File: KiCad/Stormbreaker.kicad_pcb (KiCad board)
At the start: 4 copper layers, 50.2 x 21 mm, 43 parts, among them J1 Micro_SD_Card_Det2, J2 USB_C_Receptacle_USB2.0_14P, J3 Conn_01x03, J4 FAN, Q1 PMOS, Q2 NMOS, SW1 SW_Push, U1 BQ25895RTW, U3 ATtiny1616-M

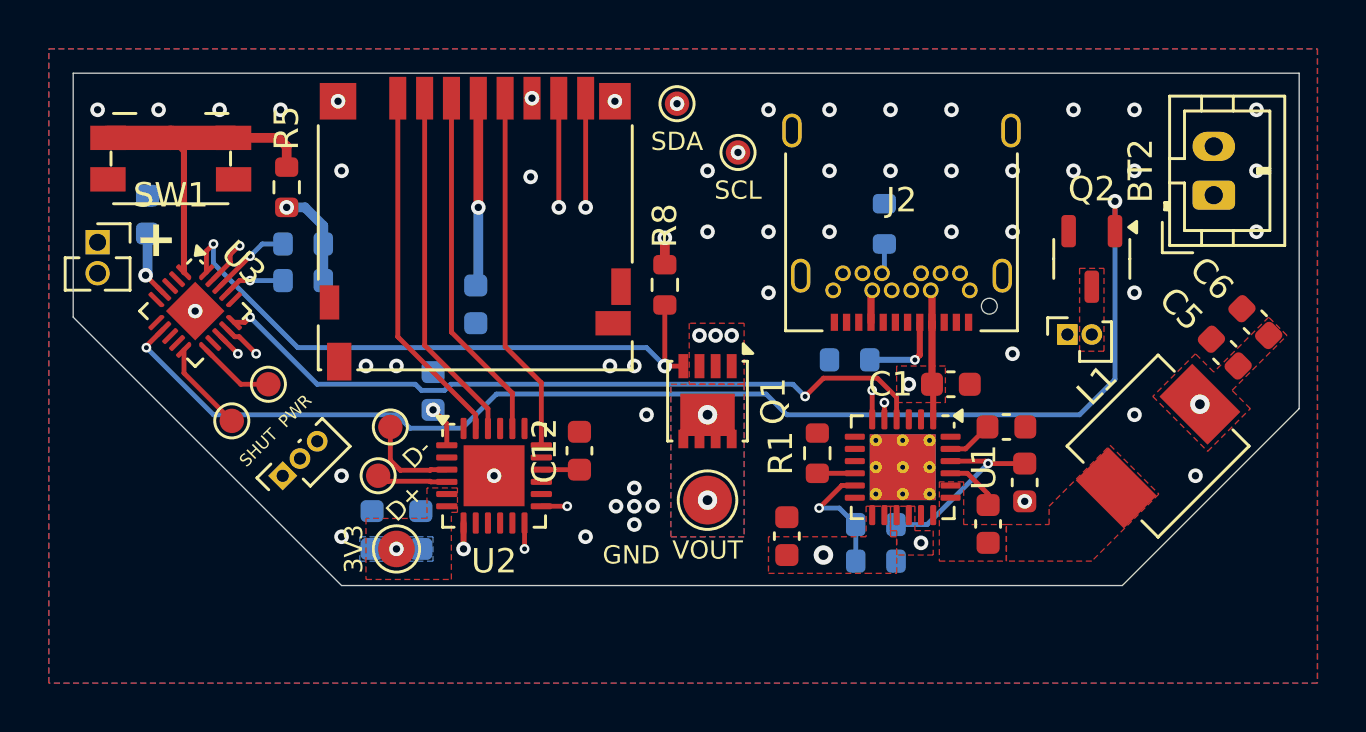
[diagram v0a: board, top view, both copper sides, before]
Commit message: More routing, via stitching, VCC zones
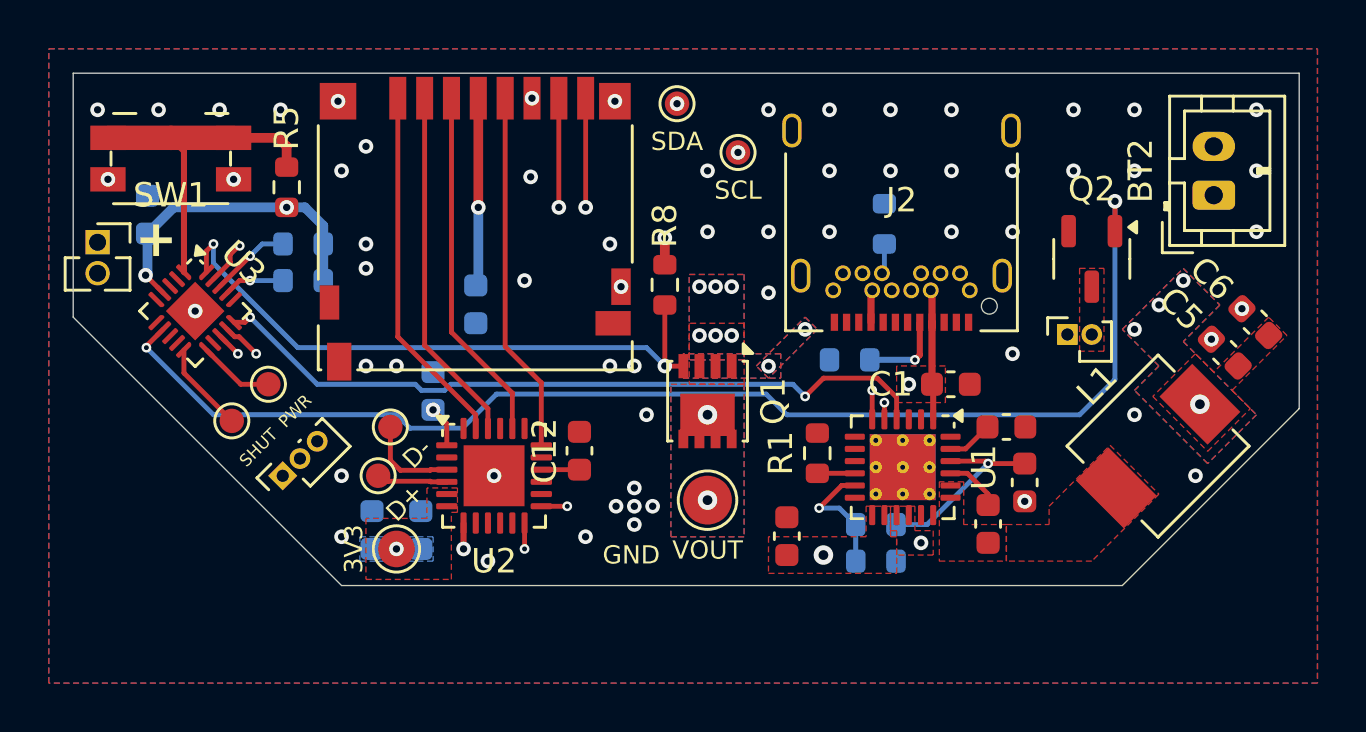
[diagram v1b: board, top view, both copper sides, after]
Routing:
- net VCC: track 7.99 -> 14.1 mm, vias 8 -> 16
- net GND: vias 51 -> 61
- added copper zone on B.Cu, net VCC
- added copper zone on In1.Cu, net VCC

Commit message: more misc changes
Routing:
- net /BATT: track 60.8 -> 61.8 mm
- net VCC: vias 16 -> 18
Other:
- outline, holes or cut-outs redrawn
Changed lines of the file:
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@@
 		(attr through_hole)
 		(fp_line
-			(start -1.33 0.635)
-			(end -1.33 1.965)
-			(stroke
-				(width 0.12)
-				(type solid)
-			)
-			(layer "F.SilkS")
-		)
-		(fp_line
-			(start -1.33 0.635)
-			(end -0.76 0.635)
-			(stroke
-				(width 0.12)
-				(type solid)
-			)
-			(layer "F.SilkS")
-		)
-		(fp_line
-			(start -1.33 1.965)
-			(end -0.30753 1.965)
-			(stroke
-				(width 0.12)
-				(type solid)
-			)
-			(layer "F.SilkS")
-		)
-		(fp_line
-			(start 0 -0.76)
-			(end 1.33 -0.76)
-			(stroke
-				(width 0.12)
-				(type solid)
-			)
-			(layer "F.SilkS")
-		)
-		(fp_line
-			(start 0.30753 1.965)
-			(end 1.33 1.965)
-			(stroke
-				(width 0.12)
-				(type solid)
-			)
-			(layer "F.SilkS")
-		)
-		(fp_line
-			(start 0.76 0.635)
-			(end 1.33 0.635)
-			(stroke
-				(width 0.12)
-				(type solid)
-			)
-			(layer "F.SilkS")
-		)
-		(fp_line
-			(start 1.33 -0.76)
-			(end 1.33 0)
-			(stroke
-				(width 0.12)
-				(type solid)
-			)
-			(layer "F.SilkS")
-		)
-		(fp_line
-			(start 1.33 0.635)
-			(end 1.33 1.965)
-			(stroke
-				(width 0.12)
-				(type solid)
-			)
-			(layer "F.SilkS")
-		)
-		(fp_line
-			(start -1.33 -1.15)
-			(end 1.33 -1.15)
+			(start -1 -1)
+			(end 1 -1)
 			(stroke
 				(width 0.05)
@@
 		)
 		(fp_line
-			(start -1.33 2.4)
-			(end -1.33 -1.15)
+			(start -1 2.25)
+			(end -1 -1)
 			(stroke
 				(width 0.05)
@@
 		)
 		(fp_line
-			(start 1.33 -1.15)
-			(end 1.33 2.4)
+			(start 1 -1)
+			(end 1 2.25)
 			(stroke
 				(width 0.05)
@@
 		)
 		(fp_line
-			(start 1.33 2.4)
-			(end -1.33 2.4)
+			(start 1 2.25)
+			(end -1 2.25)
 			(stroke
 				(width 0.05)
@@
 			(layer "F.CrtYd")
 		)
-		(fp_line
-			(start -1.27 -0.635)
-			(end 0.635 -0.635)
-			(stroke
-				(width 0.1)
-				(type solid)
-			)
-			(layer "F.Fab")
-		)
-		(fp_line
-			(start -1.27 1.905)
-			(end -1.27 -0.635)
-			(stroke
-				(width 0.1)
-				(type solid)
-			)
-			(layer "F.Fab")
-		)
-		(fp_line
-			(start 0.635 -0.635)
-			(end 1.27 0)
-			(stroke
-				(width 0.1)
-				(type solid)
-			)
-			(layer "F.Fab")
-		)
-		(fp_line
-			(start 1.27 0)
-			(end 1.27 1.905)
-			(stroke
-				(width 0.1)
-				(type solid)
-			)
-			(layer "F.Fab")
-		)
-		(fp_line
-			(start 1.27 1.905)
-			(end -1.27 1.905)
-			(stroke
-				(width 0.1)
-				(type solid)
-			)
-			(layer "F.Fab")
-		)
 		(fp_text user "${REFERENCE}"
 			(at 0 0.635 90)
@@
 	)
 	(gr_rect
-		(start 135.75 57.5)
-		(end 138.25 60)
+		(start 135.75 55.75)
+		(end 138.25 58.25)
 		(stroke
 			(width 0.1)
@@
 		(layer "F.Mask")
 	)
+	(gr_circle
+		(center 137 60.25)
+		(end 137.75 60.25)
+		(stroke
+			(width 0.05)
+			(type default)
+		)
+		(fill no)
+		(layer "Edge.Cuts")
+	)
+	(gr_circle
+		(center 141 42.25)
+		(end 141.75 42.25)
+		(stroke
+			(width 0.05)
+			(type default)
+		)
+		(fill no)
+		(layer "Edge.Cuts")
+	)
 	(gr_poly
 		(pts
@@
 		(layer "Edge.Cuts")
 	)
+	(gr_circle
+		(center 156.25 43.75)
+		(end 157.25 43.75)
+		(stroke
+			(width 0.05)
+			(type default)
+		)
+		(fill no)
+		(layer "Edge.Cuts")
+	)
 	(gr_text "GND"
-		(at 136.875 60.75 0)
+		(at 136.875 59 0)
 		(layer "F.SilkS")
 		(effects
@@
 	)
 	(via
-		(at 137 59.5)
+		(at 137 57.75)
 		(size 0.6)
 		(drill 0.3)
@@
 	)
 	(via
-		(at 137 58)
+		(at 137 56.25)
 		(size 0.6)
 		(drill 0.3)
@@
 	)
 	(via
-		(at 137 58.75)
+		(at 137 57)
 		(size 0.6)
 		(drill 0.3)
@@
 	)
 	(via
-		(at 137.75 58.75)
+		(at 137.75 57)
 		(size 0.6)
 		(drill 0.3)
@@
 	)
 	(via
-		(at 136.25 58.75)
+		(at 136.25 57)
 		(size 0.6)
 		(drill 0.3)
@@
 	)
 	(segment
-		(start 142.4 58.4)
-		(end 142.4 55.9)
+		(start 120.299 50.299)
+		(end 117.93 47.93)
 		(width 0.6)
 		(layer "In2.Cu")
@@
 	)
 	(segment
-		(start 120.299 50.299)
-		(end 117.93 47.93)
+		(start 142.4 60.15)
+		(end 142.4 55.9)
 		(width 0.6)
 		(layer "In2.Cu")
@@
 	)
 	(segment
-		(start 150.968214 59.449)
-		(end 146.051 59.449)
+		(start 123.549 50.299)
+		(end 120.299 50.299)
 		(width 0.6)
 		(layer "In2.Cu")
@@
 	)
 	(segment
-		(start 124.951 51.701)
-		(end 123.549 50.299)
+		(start 138.201 51.701)
+		(end 124.951 51.701)
 		(width 0.6)
 		(layer "In2.Cu")
@@
 	)
 	(segment
-		(start 160.75 49.667214)
-		(end 150.968214 59.449)
+		(start 150.968214 59.449)
+		(end 146.051 59.449)
 		(width 0.6)
 		(layer "In2.Cu")
@@
 	)
 	(segment
-		(start 123.549 50.299)
-		(end 120.299 50.299)
+		(start 160.75 49.667214)
+		(end 150.968214 59.449)
 		(width 0.6)
 		(layer "In2.Cu")
@@
 	)
 	(segment
-		(start 138.201 51.701)
-		(end 124.951 51.701)
+		(start 124.951 51.701)
+		(end 123.549 50.299)
 		(width 0.6)
 		(layer "In2.Cu")
@@
 	(segment
 		(start 144.75 60.75)
-		(end 142.4 58.4)
+		(end 143 60.75)
 		(width 0.6)
 		(layer "In2.Cu")
@@
 	)
 	(segment
-		(start 142.4 55.9)
-		(end 138.201 51.701)
+		(start 143 60.75)
+		(end 142.4 60.15)
 		(width 0.6)
 		(layer "In2.Cu")
@@
 	)
 	(segment
+		(start 142.4 55.9)
+		(end 138.201 51.701)
+		(width 0.6)
+		(layer "In2.Cu")
+		(net 2)
+	)
+	(segment
 		(start 149.25 53.8)
 		(end 149.2 53.75)
@@
 	)
 	(via
+		(at 161.75 53)
+		(size 0.6)
+		(drill 0.3)
+		(layers "F.Cu" "B.Cu")
+		(net 7)
+	)
+	(via
 		(at 158.5 50.5)
 		(size 0.6)
@@
 		(net 7)
 	)
+	(via
+		(at 163 51.75)
+		(size 0.6)
+		(drill 0.3)
+		(layers "F.Cu" "B.Cu")
+		(net 7)
+	)
 	(segment
 		(start 118.121016 46.5)
@@
 			(pts
 				(xy 154 58.75) (xy 156.5 56.25) (xy 158.5 58.25) (xy 155.75 61) (xy 152.25 61) (xy 152.25 59.5)
-				(xy 154 59.5)
+				(xy 153.25 59.5)
 			)
 		)
@@
 		(polygon
 			(pts
-				(xy 149.5 57.75) (xy 149.5 61) (xy 152.25 61) (xy 152.25 59.5) (xy 150.5 59.5) (xy 150.5 57.75)
+				(xy 149.5 57.75) (xy 149.5 61) (xy 152.25 61) (xy 152.25 59.5) (xy 150.75 59.5) (xy 150.5 59.25)
+				(xy 150.5 57.75)
 			)
 		)

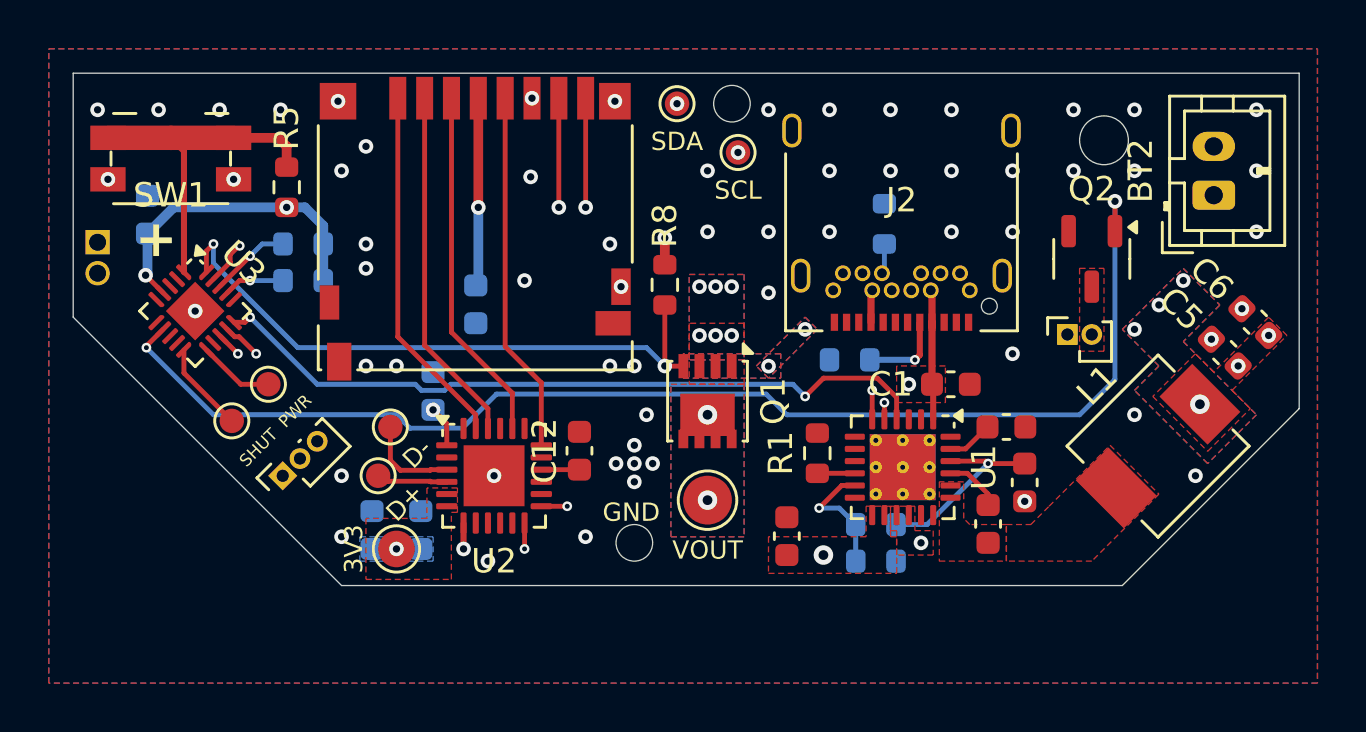
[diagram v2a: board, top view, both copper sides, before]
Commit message: Add point for neopixel
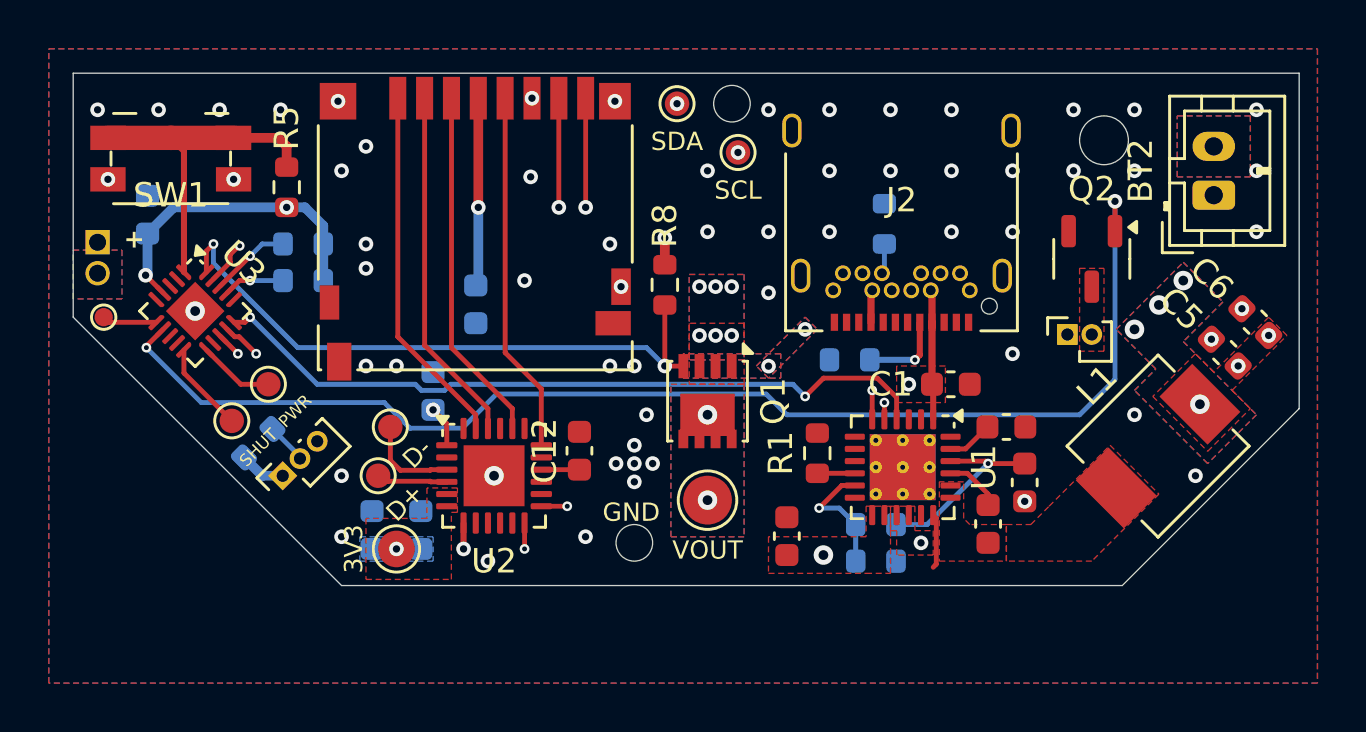
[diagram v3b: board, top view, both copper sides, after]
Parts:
- added R7: 1k, Resistor_SMD:R_0603_1608Metric, B.Cu at (121.6, 56.2)
- added TP10: LED, TestPoint:TestPoint_Pad_D1.0mm, F.Cu at (115.2, 51.0)
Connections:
- U3 pad 6: unconnected-(U3-PA5-Pad6) -> /LED
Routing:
- net /LED: track 0.00 -> 2.25 mm
- net GND: track 0.00 -> 2.24 mm
- net VCC: track 14.1 -> 16.0 mm
- net /PA0: track 12.6 -> 13.9 mm

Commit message: more minor misc modifications
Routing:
- net /PowerButton: track 14.1 -> 15.1 mm
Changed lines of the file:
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@@
-	)
-	(segment
-		(start 118.121016 46.5)
-		(end 117.048008 47.573008)
-		(width 0.4)
-		(layer "B.Cu")
-		(net 7)
 	)
 	(segment
@@
 	)
 	(segment
-		(start 122.75 46.5)
-		(end 118.121016 46.5)
-		(width 0.4)
-		(layer "B.Cu")
-		(net 7)
-	)
-	(segment
 		(start 122.587833 57.502046)
 		(end 121.752046 57.502046)
@@
 	(segment
 		(start 122.75 46.5)
+		(end 119.75 46.5)
+		(width 0.4)
+		(layer "B.Cu")
+		(net 7)
+	)
+	(segment
+		(start 122.75 46.5)
 		(end 123.5 46.5)
+		(width 0.4)
+		(layer "B.Cu")
+		(net 7)
+	)
+	(segment
+		(start 118.676992 47.573008)
+		(end 117.048008 47.573008)
 		(width 0.4)
 		(layer "B.Cu")
@@
 		(start 117.048008 47.573008)
 		(end 117.048008 49.201992)
+		(width 0.4)
+		(layer "B.Cu")
+		(net 7)
+	)
+	(segment
+		(start 119.75 46.5)
+		(end 118.676992 47.573008)
 		(width 0.4)
 		(layer "B.Cu")
@@
 	)
 	(segment
-		(start 118 43.65)
+		(start 119.8375 43.65)
 		(end 120.575 43.65)
+		(width 0.2)
+		(layer "F.Cu")
+		(net 48)
+	)
+	(segment
+		(start 120.575 43.65)
+		(end 115.425 43.65)
 		(width 1)
 		(layer "F.Cu")
@@
 	)
 	(segment
-		(start 118.540381 44.190381)
-		(end 118 43.65)
-		(width 0.25)
-		(layer "F.Cu")
-		(net 48)
-	)
-	(segment
-		(start 115.425 43.65)
-		(end 118 43.65)
-		(width 1)
+		(start 118.540381 44.947119)
+		(end 119.8375 43.65)
+		(width 0.2)
 		(layer "F.Cu")
 		(net 48)
@@
 	(segment
 		(start 118.540381 49.15901)
-		(end 118.540381 44.190381)
-		(width 0.25)
+		(end 118.540381 44.947119)
+		(width 0.2)
 		(layer "F.Cu")
 		(net 48)
@@
 			(pts
 				(xy 147.5 58.75) (xy 146.5 58.75) (xy 146.5 60) (xy 142.5 60) (xy 142.5 61.5) (xy 146.5 61.5) (xy 147.5 61.5)
-				(xy 147.5 60) (xy 147.5 60)
+				(xy 147.5 60)
 			)
 		)

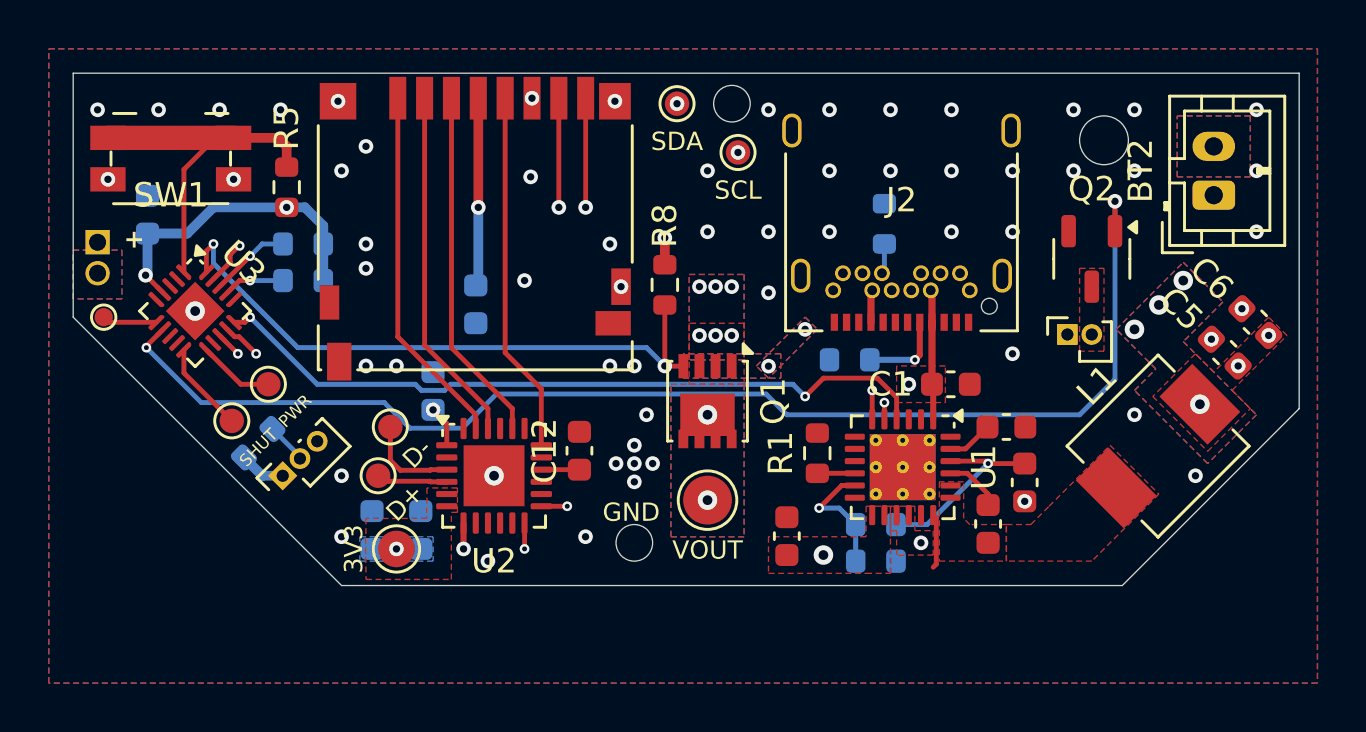
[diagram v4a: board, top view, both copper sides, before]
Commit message: Redo power and BQ layout and routing
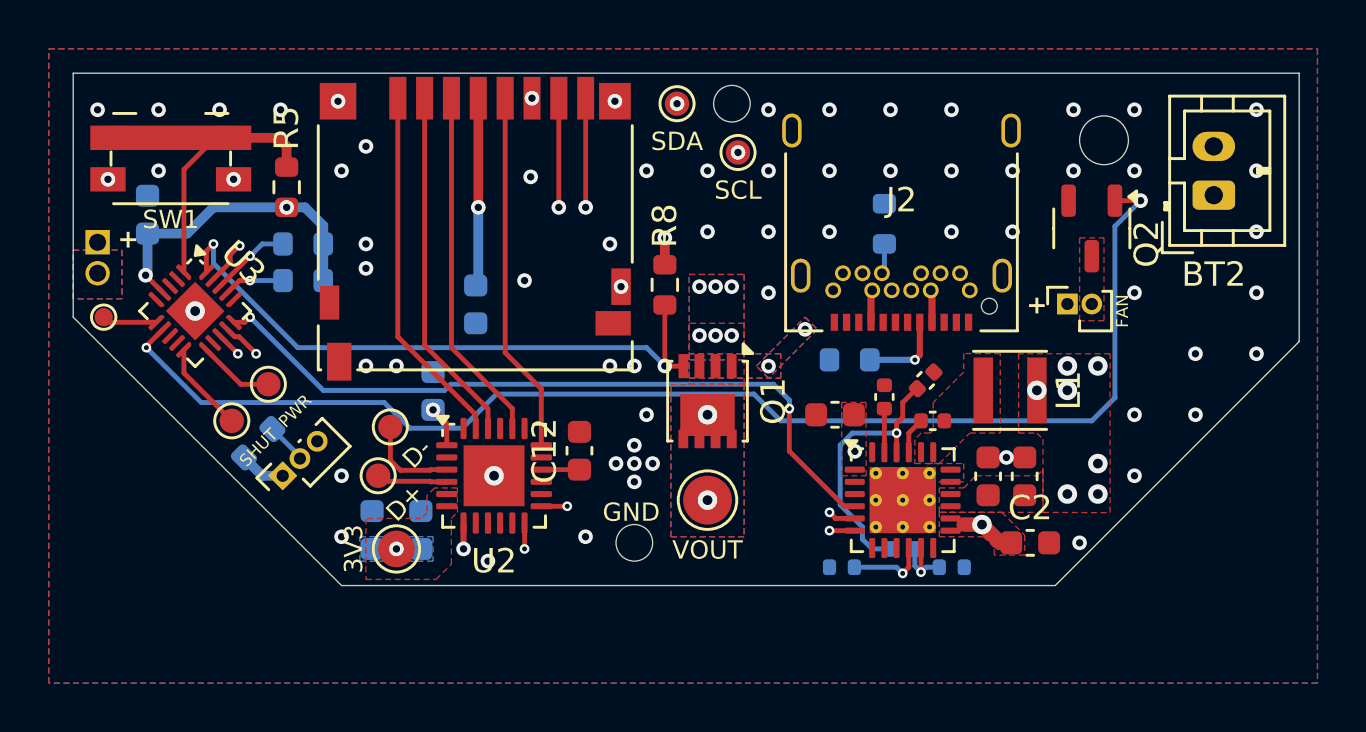
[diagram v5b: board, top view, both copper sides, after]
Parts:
- C3, C4: footprint Capacitor_SMD:C_0603_1608Metric -> Capacitor_SMD:C_0402_1005Metric
- C7: value 40uF -> 60uF; footprint Capacitor_SMD:C_0603_1608Metric -> Capacitor_SMD:C_0402_1005Metric
- L1: value 2.2uH -> 1uH; footprint Inductor_SMD:L_Vishay_IHLP-2020 -> Inductor_SMD:L_Taiyo-Yuden_MD-3030
- R1: footprint Resistor_SMD:R_0603_1608Metric -> Resistor_SMD:R_0402_1005Metric; moved to B.Cu
- R2, R3: footprint Resistor_SMD:R_0603_1608Metric -> Resistor_SMD:R_0402_1005Metric
- moved C6 11.4 mm to (153.0, 57.5), turned to 90 degrees
- moved C5 10.9 mm to (151.5, 57.5), turned to 90 degrees
- moved C2 9.98 mm to (153.2, 60.2), turned to 0 degrees
- moved L1 6.48 mm to (152.4, 54.0), turned to 0 degrees
- moved C4 5.83 mm to (148.9, 53.6), turned to -135 degrees
- moved C7 5.15 mm to (147.2, 54.3), turned to -90 degrees
- moved C1 4.91 mm to (145.2, 55.0), turned to 180 degrees
- moved C3 4.80 mm to (149.2, 55.2), turned to 180 degrees
- moved R1 4.78 mm to (145.5, 61.2), turned to 0 degrees
- moved R2 3.12 mm to (150.0, 61.2)
- moved R3 1.48 mm to (148.0, 60.5), turned to 180 degrees
- moved U1 1.35 mm to (148.0, 58.5), turned to 0 degrees
- moved J4 1.25 mm to (154.8, 50.5)
- moved Q2 1.25 mm to (155.8, 47.4)
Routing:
- net SDA_2: track 31.1 -> 34.6 mm
- net Net-(U1-REGN): track 7.89 -> 11.0 mm
- net SCL_2: track 32.9 -> 35.6 mm
- net Net-(U1-TS): track 5.13 -> 2.87 mm
- net GND: track 2.24 -> 0.00 mm, vias 61 -> 67
- net /BATT: track 61.8 -> 63.5 mm
- net Net-(U1-ILIM): track 1.54 -> 3.22 mm, vias 0 -> 1
- net Net-(Q2-G): track 52.2 -> 53.1 mm
- net Net-(U1-BTST): track 2.34 -> 1.55 mm
- net VBUS: track 13.8 -> 13.0 mm
- removed copper zone on In2.Cu, net VBUS
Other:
- outline, holes or cut-outs redrawn
